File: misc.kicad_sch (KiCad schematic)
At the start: 1 part, among them U1 MIMX8MN5DVPIZAA

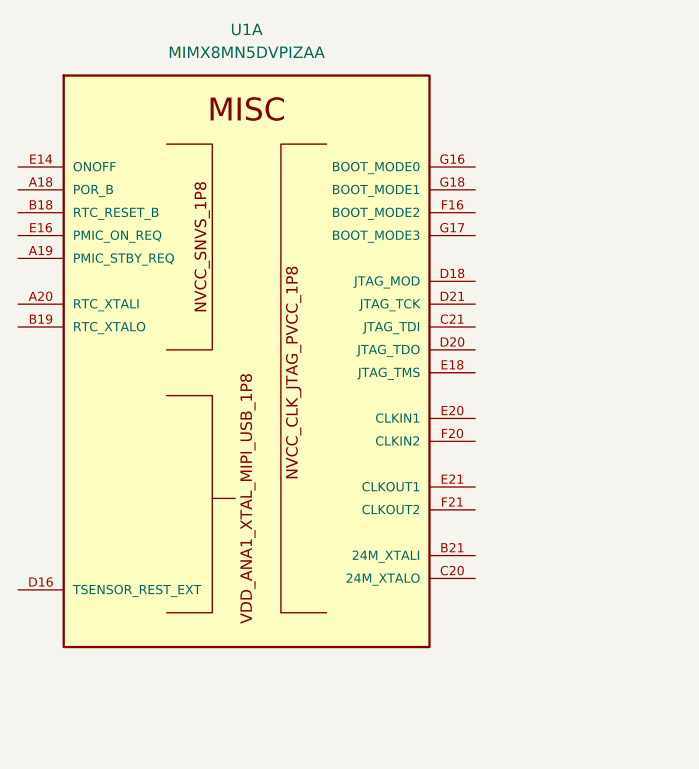
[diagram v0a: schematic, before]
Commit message: move to i.MX8M Mini
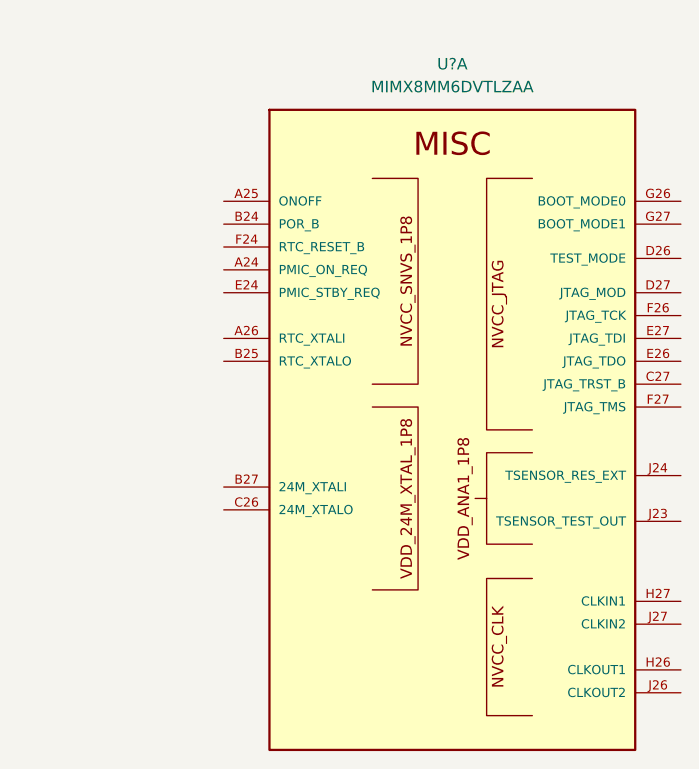
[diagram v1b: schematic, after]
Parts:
- removed U1: MIMX8MN5DVPIZAA, qsbc:SOT1967-1, symbol qsbc:MIMX8MN5DVPIZAA
- added U?: MIMX8MM6DVTLZAA, qsbc:SOT1967-1, symbol qsbc:MIMX8MM6DVTLZAA

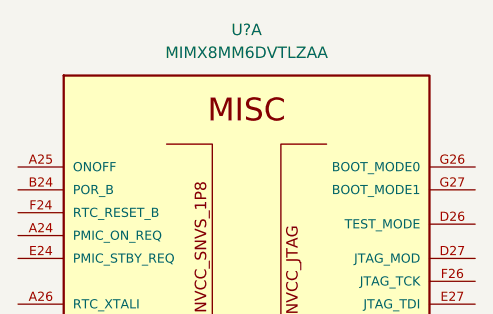
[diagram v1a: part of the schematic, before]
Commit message: ddr sch done
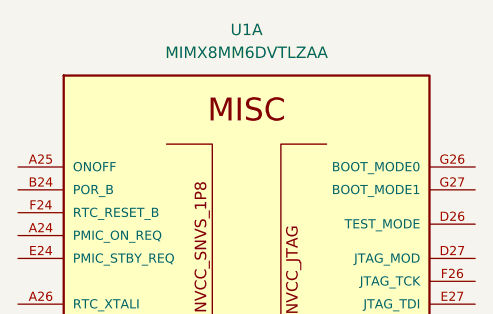
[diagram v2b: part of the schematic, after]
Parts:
- gave numbers to parts that had none: 1
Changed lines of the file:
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@@
   (symbol (lib_id "qsbc:MIMX8MM6DVTLZAA") (at 149.86 76.2 0) (unit 1)
     (in_bom yes) (on_board yes) (fields_autoplaced)
-    (property "Reference" "U?" (id 0) (at 149.86 57.15 0))
+    (property "Reference" "U1" (id 0) (at 149.86 57.15 0))
     (property "Value" "MIMX8MM6DVTLZAA" (id 1) (at 149.86 59.69 0))
     (property "Footprint" "qsbc:SOT1967-1" (id 2) (at 153.67 266.7 0)

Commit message: misc work, usb sch done
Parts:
- added J6: Conn_ARM_JTAG_SWD_10, symbol Connector:Conn_ARM_JTAG_SWD_10
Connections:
- new net: J6.3 (GND), J6.5 (GND)
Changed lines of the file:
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@@
     (pin "D19")
   )
+  (symbol (lib_id "Connector:Conn_ARM_JTAG_SWD_10") (at 237.49 85.09 0) (unit 1)
+    (in_bom yes) (on_board yes) (fields_autoplaced)
+    (property "Reference" "J6" (id 0) (at 226.06 83.8199 0)
+      (effects (font (size 1.27 1.27)) (justify right))
+    )
+    (property "Value" "Conn_ARM_JTAG_SWD_10" (id 1) (at 226.06 86.3599 0)
+      (effects (font (size 1.27 1.27)) (justify right))
+    )
+    (property "Footprint" "" (id 2) (at 237.49 85.09 0)
+      (effects (font (size 1.27 1.27)) hide)
+    )
+    (property "Datasheet" "http://infocenter.arm.com/help/topic/com.arm.doc.ddi0314h/DDI0314H_coresight_components_trm.pdf" (id 3) (at 228.6 116.84 90)
+      (effects (font (size 1.27 1.27)) hide)
+    )
+    (pin "1")
+    (pin "10")
+    (pin "2")
+    (pin "3")
+    (pin "4")
+    (pin "5")
+    (pin "6")
+    (pin "7")
+    (pin "8")
+    (pin "9")
+  )
 )

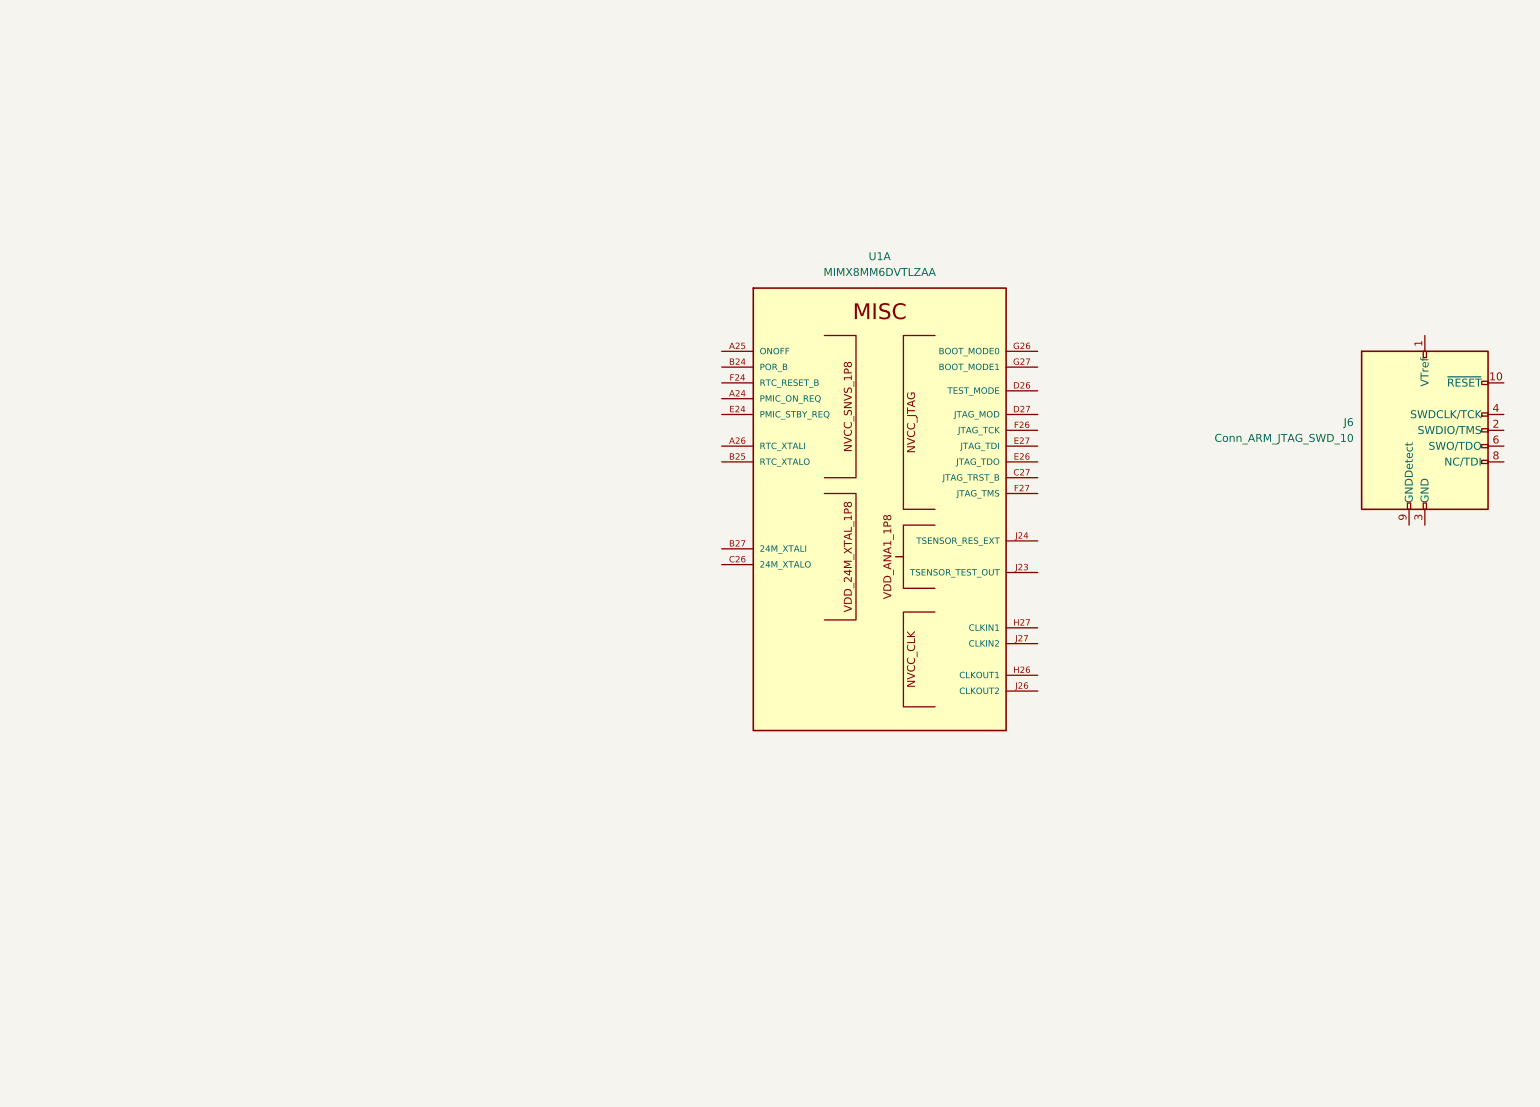
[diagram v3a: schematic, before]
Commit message: ddr: add dual die support, misc work
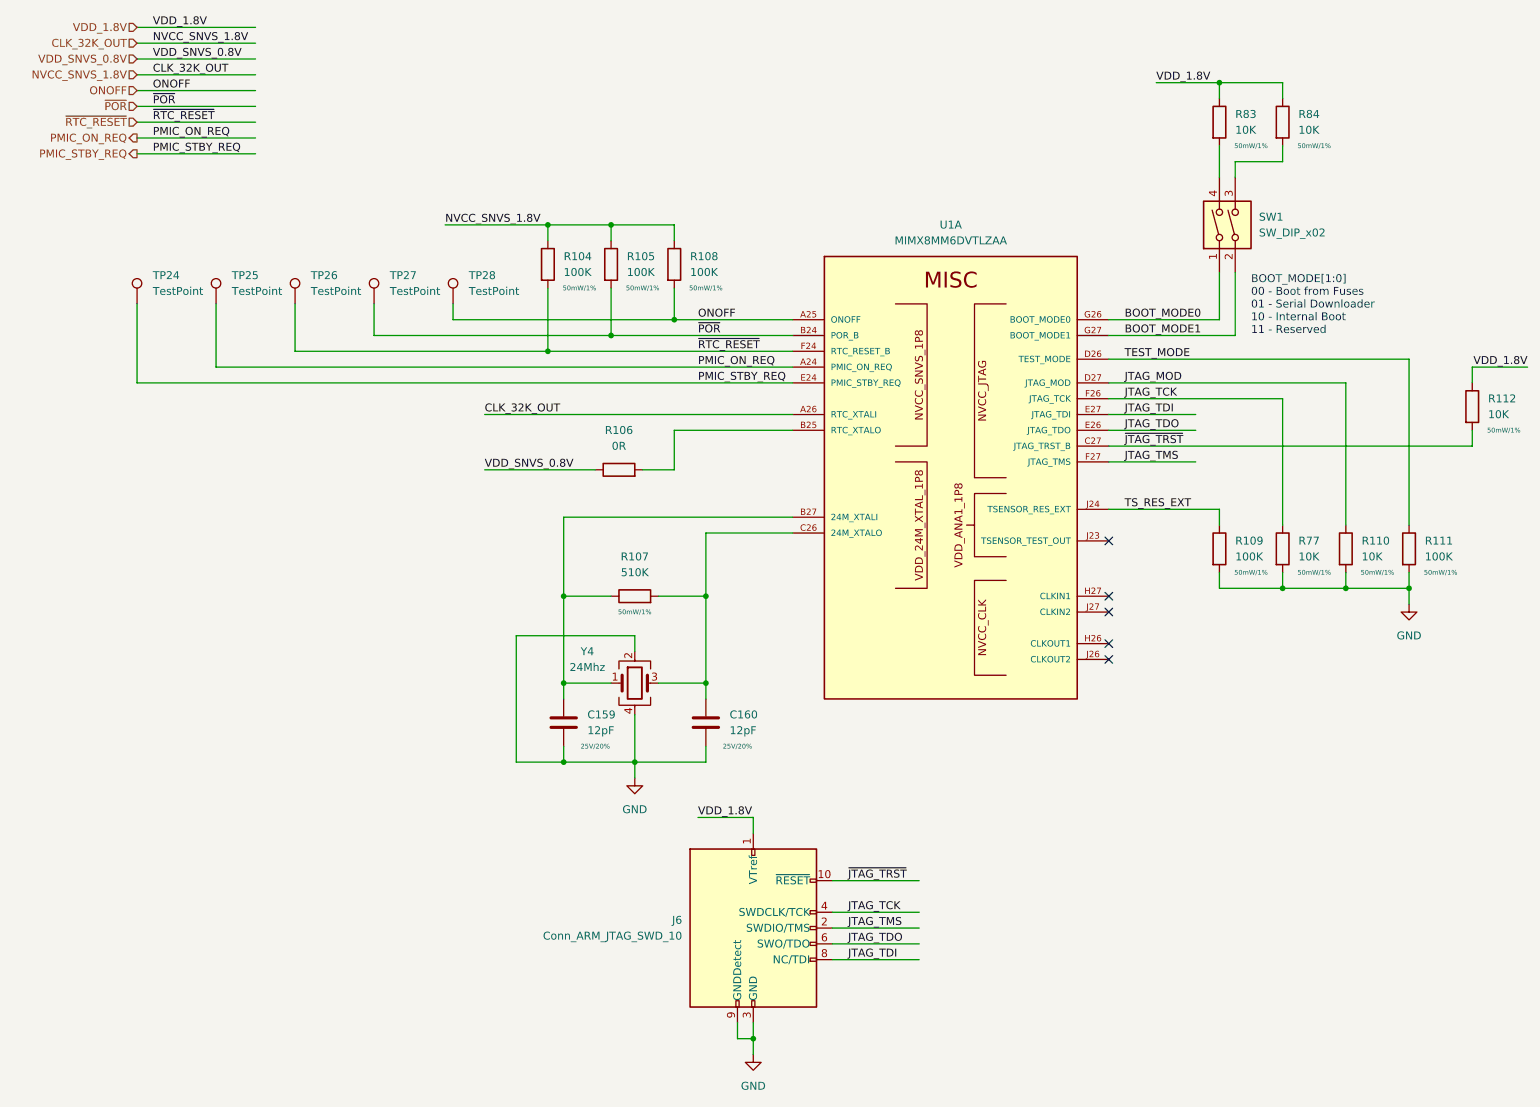
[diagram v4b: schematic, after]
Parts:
- added C159, C160: 12pF, Capacitor_SMD:C_0402_1005Metric, symbol Device:C
- added R104, R105, R108, R109, R111: 100K, Resistor_SMD:R_0402_1005Metric, symbol Device:R
- added R106: 0R, Resistor_SMD:R_0402_1005Metric, symbol Device:R
- added R107: 510K, Resistor_SMD:R_0402_1005Metric, symbol Device:R
- added R110, R112, R77, R83, R84: 10K, Resistor_SMD:R_0402_1005Metric, symbol Device:R
- added SW1: SW_DIP_x02, qsbc:DHN-02, symbol Switch:SW_DIP_x02
- added TP24, TP25, TP26, TP27, TP28: TestPoint, TestPoint:TestPoint_Pad_D1.0mm, symbol Connector:TestPoint
- added Y4: 24Mhz, Crystal:Crystal_SMD_3225-4Pin_3.2x2.5mm, symbol Device:Crystal_GND24
- J6: footprint (none) -> Connector_PinHeader_1.27mm:PinHeader_2x05_P1.27mm_Vertical
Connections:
- net PMIC_ON_REQ: now reaches U1.A24 (PMIC_ON_REQ)
- net PMIC_ON_REQ: now also TP25.1
- net ONOFF: now reaches U1.A25 (ONOFF)
- net ONOFF: now also R108.2, TP28.1
- net CLK_32K_OUT: now reaches U1.A26 (RTC_XTALI)
- net CLK_32K_OUT: now also R104.1, R105.1, R108.1
- net ~{POR}: now reaches U1.B24 (POR_B)
- net ~{POR}: now also R105.2, TP27.1
- net at U1.B25 (RTC_XTALO): now also R106.2
- net at U1.B27 (24M_XTALI): now also C159.1, R107.1, Y4.1
- net at U1.C26 (24M_XTALO): now also C160.1, R107.2, Y4.3
- net ~{JTAG_TRST}: now reaches U1.C27 (JTAG_TRST_B)
- net ~{JTAG_TRST}: now also J6.10 (~{RESET}), R112.2
- net TEST_MODE: now reaches U1.D26 (TEST_MODE)
- net TEST_MODE: now also R111.1
- net JTAG_MOD: now reaches U1.D27 (JTAG_MOD)
- net JTAG_MOD: now also R110.1
- net PMIC_STBY_REQ: now reaches U1.E24 (PMIC_STBY_REQ)
- net PMIC_STBY_REQ: now also TP24.1
- net JTAG_TDO: now reaches U1.E26 (JTAG_TDO)
- net JTAG_TDO: now also J6.6 (SWO/TDO)
- net JTAG_TDI: now reaches U1.E27 (JTAG_TDI)
- net JTAG_TDI: now also J6.8 (NC/TDI)
- net ~{RTC_RESET}: now reaches U1.F24 (RTC_RESET_B)
- net ~{RTC_RESET}: now also R104.2, TP26.1
- net JTAG_TCK: now reaches U1.F26 (JTAG_TCK)
- net JTAG_TCK: now also J6.4 (SWDCLK/TCK), R77.1
- net JTAG_TMS: now reaches U1.F27 (JTAG_TMS)
- net JTAG_TMS: now also J6.2 (SWDIO/TMS)
- net BOOT_MODE0: now reaches U1.G26 (BOOT_MODE0)
- net BOOT_MODE0: now also SW1.1
- net BOOT_MODE1: now reaches U1.G27 (BOOT_MODE1)
- net BOOT_MODE1: now also SW1.2
- net TS_RES_EXT: now reaches U1.J24 (TSENSOR_RES_EXT)
- net TS_RES_EXT: now also R109.1
- net VDD_1.8V: now reaches J6.1 (VTref)
- net VDD_1.8V: now also R112.1, R83.1, R84.1
- net GND: now reaches J6.3 (GND), J6.5 (GND)
- net GND: now also J6.9 (GNDDetect), C159.2, C160.2, R109.2, R110.2, R111.2, R77.2, Y4.2, Y4.4
- new net: R84.2, SW1.3
- new net: R83.2, SW1.4
- new net VDD_SNVS_0.8V: R106.1
- no-connect marks 0 -> 5
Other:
- note added: "BOOT_MODE[1:0] 00 - Boot from Fuses 01 - Serial Downloader 10 - Internal Boot 11 - Reserved"
- company: (none) -> Q-LAB
- title: (none) -> QSBC
- moved on the sheet: J6, U1A
